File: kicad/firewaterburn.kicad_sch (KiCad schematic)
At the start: 7 parts, among them P101 USB_C_Plug_USB2.0, U101 TPD4E02B04DQA

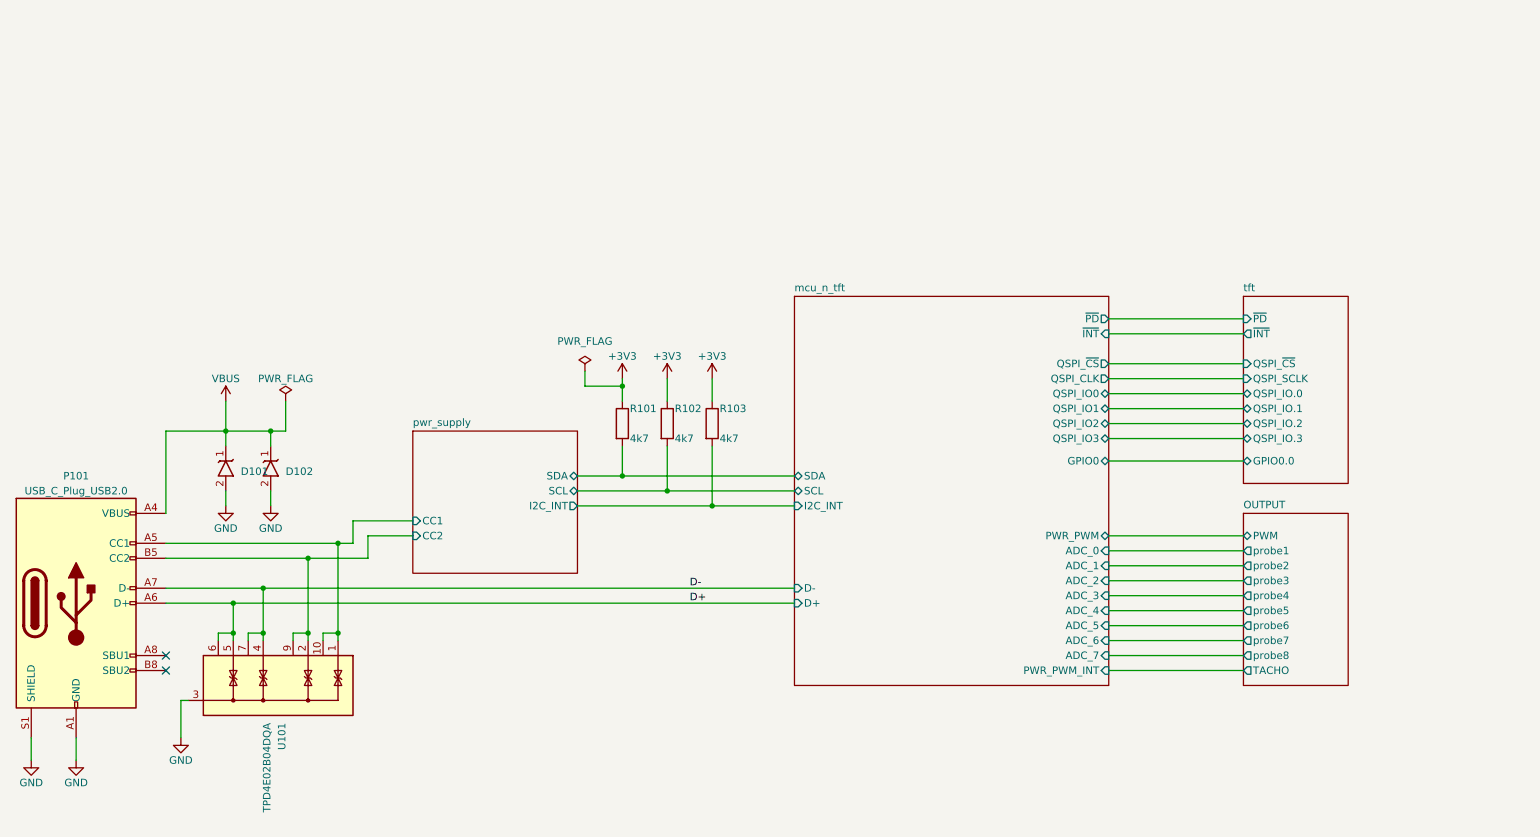
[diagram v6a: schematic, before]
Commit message: add nrf52840 board
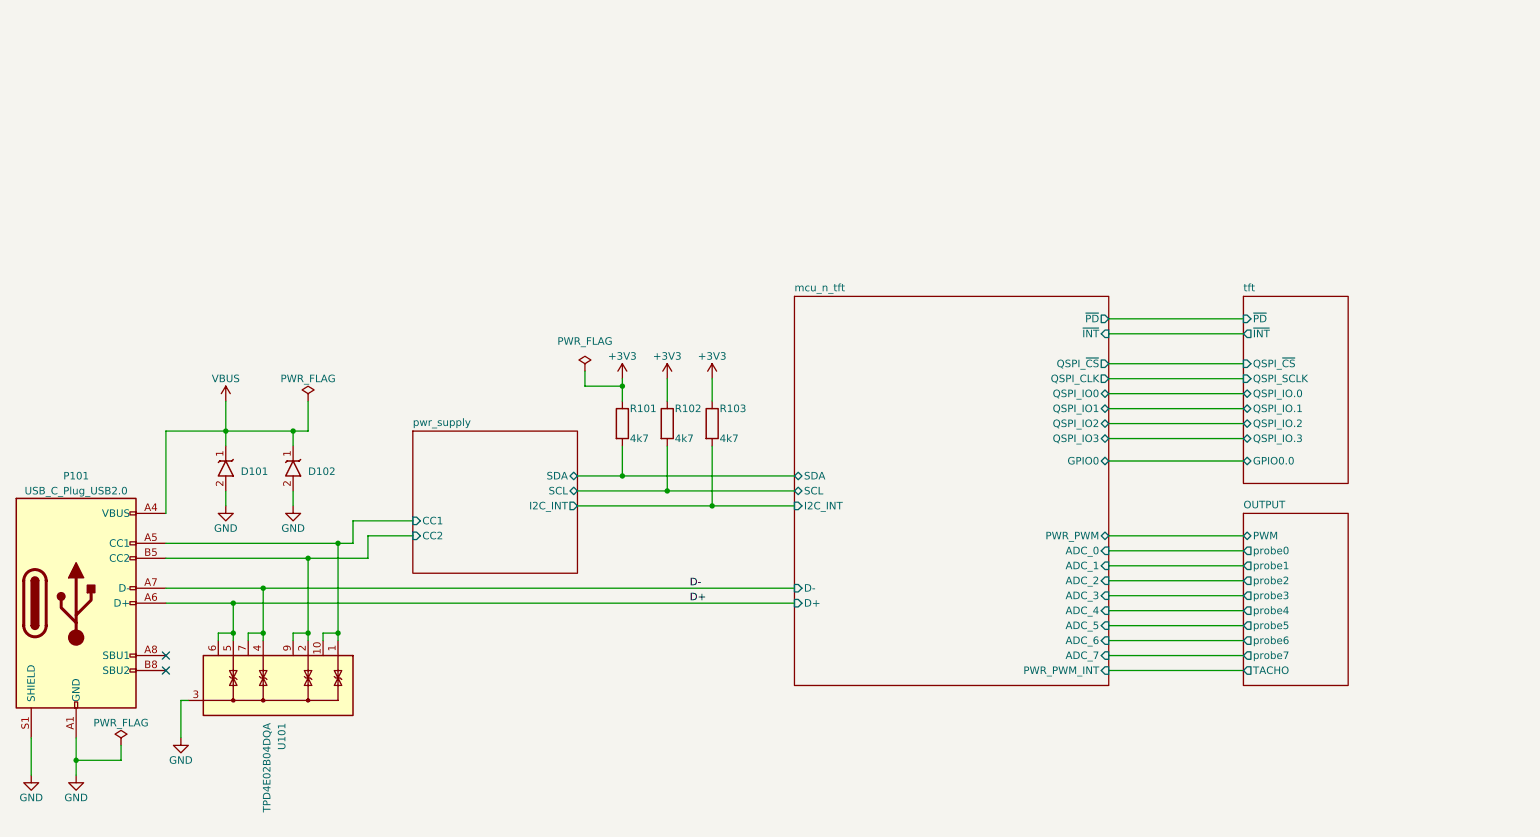
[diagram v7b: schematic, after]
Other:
- sheet OUTPUT ports: added probe0; removed probe8
- moved on the sheet: D102
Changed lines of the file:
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@@
   (junction (at 121.92 87.63) (diameter 0) (color 0 0 0 0)
   )
-  (junction (at 62.23 95.25) (diameter 0) (color 0 0 0 0)
+  (junction (at 29.21 151.13) (diameter 0) (color 0 0 0 0)
+  )
+  (junction (at 66.04 95.25) (diameter 0) (color 0 0 0 0)
   )
   (junction (at 137.16 107.95) (diameter 0) (color 0 0 0 0)
@@
     (stroke (width 0) (type default))
   )
-  (wire (pts (xy 21.59 151.13) (xy 21.59 147.32))
+  (wire (pts (xy 21.59 153.67) (xy 21.59 147.32))
     (stroke (width 0) (type default))
   )
@@
     (stroke (width 0) (type default))
   )
-  (wire (pts (xy 62.23 95.25) (xy 62.23 97.79))
+  (wire (pts (xy 66.04 95.25) (xy 66.04 97.79))
     (stroke (width 0) (type default))
   )
@@
     (stroke (width 0) (type default))
   )
-  (wire (pts (xy 62.23 105.41) (xy 62.23 107.95))
+  (wire (pts (xy 66.04 105.41) (xy 66.04 107.95))
+    (stroke (width 0) (type default))
+  )
+  (wire (pts (xy 36.83 148.59) (xy 36.83 151.13))
     (stroke (width 0) (type default))
   )
@@
     (stroke (width 0) (type default))
   )
+  (wire (pts (xy 29.21 151.13) (xy 36.83 151.13))
+    (stroke (width 0) (type default))
+  )
   (wire (pts (xy 60.96 129.54) (xy 60.96 130.81))
     (stroke (width 0) (type default))
@@
     (stroke (width 0) (type default))
   )
-  (wire (pts (xy 62.23 95.25) (xy 54.61 95.25))
+  (wire (pts (xy 66.04 95.25) (xy 54.61 95.25))
     (stroke (width 0) (type default))
   )
@@
     (stroke (width 0) (type default))
   )
-  (wire (pts (xy 64.77 95.25) (xy 62.23 95.25))
+  (wire (pts (xy 68.58 95.25) (xy 66.04 95.25))
     (stroke (width 0) (type default))
   )
@@
     (stroke (width 0) (type default))
   )
-  (wire (pts (xy 64.77 90.17) (xy 64.77 95.25))
+  (wire (pts (xy 68.58 90.17) (xy 68.58 95.25))
     (stroke (width 0) (type default))
   )
@@
   )
   (wire (pts (xy 44.45 95.25) (xy 54.61 95.25))
+    (stroke (width 0) (type default))
+  )
+  (wire (pts (xy 29.21 151.13) (xy 29.21 153.67))
     (stroke (width 0) (type default))
   )
@@
     )
   )
-  (symbol (lib_id "power:GND") (at 29.21 151.13 0) (unit 1)
-    (in_bom yes) (on_board yes) (dnp no)
-    (property "Reference" "#PWR0109" (at 29.21 157.48 0)
-      (effects (font (size 1.27 1.27)) hide)
-    )
-    (property "Value" "GND" (at 29.21 154.94 0)
-      (effects (font (size 1.27 1.27)))
-    )
-    (property "Footprint" "" (at 29.21 151.13 0)
-      (effects (font (size 1.27 1.27)) hide)
-    )
-    (property "Datasheet" "" (at 29.21 151.13 0)
+  (symbol (lib_id "power:GND") (at 29.21 153.67 0) (unit 1)
+    (in_bom yes) (on_board yes) (dnp no)
+    (property "Reference" "#PWR0109" (at 29.21 160.02 0)
+      (effects (font (size 1.27 1.27)) hide)
+    )
+    (property "Value" "GND" (at 29.21 157.48 0)
+      (effects (font (size 1.27 1.27)))
+    )
+    (property "Footprint" "" (at 29.21 153.67 0)
+      (effects (font (size 1.27 1.27)) hide)
+    )
+    (property "Datasheet" "" (at 29.21 153.67 0)
       (effects (font (size 1.27 1.27)) hide)
     )
@@
     )
   )
-  (symbol (lib_id "power:GND") (at 21.59 151.13 0) (unit 1)
-    (in_bom yes) (on_board yes) (dnp no)
-    (property "Reference" "#PWR0108" (at 21.59 157.48 0)
-      (effects (font (size 1.27 1.27)) hide)
-    )
-    (property "Value" "GND" (at 21.59 154.94 0)
-      (effects (font (size 1.27 1.27)))
-    )
-    (property "Footprint" "" (at 21.59 151.13 0)
-      (effects (font (size 1.27 1.27)) hide)
-    )
-    (property "Datasheet" "" (at 21.59 151.13 0)
+  (symbol (lib_id "power:GND") (at 21.59 153.67 0) (unit 1)
+    (in_bom yes) (on_board yes) (dnp no)
+    (property "Reference" "#PWR0108" (at 21.59 160.02 0)
+      (effects (font (size 1.27 1.27)) hide)
+    )
+    (property "Value" "GND" (at 21.59 157.48 0)
+      (effects (font (size 1.27 1.27)))
+    )
+    (property "Footprint" "" (at 21.59 153.67 0)
+      (effects (font (size 1.27 1.27)) hide)
+    )
+    (property "Datasheet" "" (at 21.59 153.67 0)
       (effects (font (size 1.27 1.27)) hide)
     )
@@
     )
   )
-  (symbol (lib_id "power:PWR_FLAG") (at 64.77 90.17 0) (unit 1)
-    (in_bom yes) (on_board yes) (dnp no)
-    (property "Reference" "#FLG0102" (at 64.77 88.265 0)
-      (effects (font (size 1.27 1.27)) hide)
-    )
-    (property "Value" "PWR_FLAG" (at 64.77 86.36 0)
-      (effects (font (size 1.27 1.27)))
-    )
-    (property "Footprint" "" (at 64.77 90.17 0)
-      (effects (font (size 1.27 1.27)) hide)
-    )
-    (property "Datasheet" "~" (at 64.77 90.17 0)
+  (symbol (lib_id "power:PWR_FLAG") (at 68.58 90.17 0) (unit 1)
+    (in_bom yes) (on_board yes) (dnp no)
+    (property "Reference" "#FLG0102" (at 68.58 88.265 0)
+      (effects (font (size 1.27 1.27)) hide)
+    )
+    (property "Value" "PWR_FLAG" (at 68.58 86.36 0)
+      (effects (font (size 1.27 1.27)))
+    )
+    (property "Footprint" "" (at 68.58 90.17 0)
+      (effects (font (size 1.27 1.27)) hide)
+    )
+    (property "Datasheet" "~" (at 68.58 90.17 0)
       (effects (font (size 1.27 1.27)) hide)
     )
@@
     )
   )
-  (symbol (lib_id "mylib_ic:ESDA25P35") (at 62.23 101.6 270) (unit 1)
+  (symbol (lib_id "mylib_ic:ESDA25P35") (at 66.04 101.6 270) (unit 1)
     (in_bom yes) (on_board yes) (dnp no) (fields_autoplaced)
-    (property "Reference" "D102" (at 64.77 102.108 90)
-      (effects (font (size 1.27 1.27)) (justify left))
-    )
-    (property "Value" "ESDA25P35" (at 59.69 101.6 0)
-      (effects (font (size 1.27 1.27)) hide)
-    )
-    (property "Footprint" "mylib_ic:D_0604_1610Metric" (at 62.23 101.6 0)
-      (effects (font (size 1.27 1.27)) hide)
-    )
-    (property "Datasheet" "" (at 62.23 101.6 0)
-      (effects (font (size 1.27 1.27)) hide)
-    )
-    (property "Digikey" "497-16913-1-ND" (at 62.23 101.6 90)
+    (property "Reference" "D102" (at 68.58 102.108 90)
+      (effects (font (size 1.27 1.27)) (justify left))
+    )
+    (property "Value" "ESDA25P35" (at 63.5 101.6 0)
+      (effects (font (size 1.27 1.27)) hide)
+    )
+    (property "Footprint" "mylib_ic:D_0604_1610Metric" (at 66.04 101.6 0)
+      (effects (font (size 1.27 1.27)) hide)
+    )
+    (property "Datasheet" "" (at 66.04 101.6 0)
+      (effects (font (size 1.27 1.27)) hide)
+    )
+    (property "Digikey" "497-16913-1-ND" (at 66.04 101.6 90)
       (effects (font (size 1.27 1.27)) hide)
     )
@@
     )
   )
-  (symbol (lib_id "power:GND") (at 62.23 107.95 0) (unit 1)
-    (in_bom yes) (on_board yes) (dnp no)
-    (property "Reference" "#PWR0106" (at 62.23 114.3 0)
-      (effects (font (size 1.27 1.27)) hide)
-    )
-    (property "Value" "GND" (at 62.23 111.76 0)
-      (effects (font (size 1.27 1.27)))
-    )
-    (property "Footprint" "" (at 62.23 107.95 0)
-      (effects (font (size 1.27 1.27)) hide)
-    )
-    (property "Datasheet" "" (at 62.23 107.95 0)
+  (symbol (lib_id "power:GND") (at 66.04 107.95 0) (unit 1)
+    (in_bom yes) (on_board yes) (dnp no)
+    (property "Reference" "#PWR0106" (at 66.04 114.3 0)
+      (effects (font (size 1.27 1.27)) hide)
+    )
+    (property "Value" "GND" (at 66.04 111.76 0)
+      (effects (font (size 1.27 1.27)))
+    )
+    (property "Footprint" "" (at 66.04 107.95 0)
+      (effects (font (size 1.27 1.27)) hide)
+    )
+    (property "Datasheet" "" (at 66.04 107.95 0)
       (effects (font (size 1.27 1.27)) hide)
     )
@@
         (path "/e63e39d7-6ac0-4ffd-8aa3-1841a4541b55"
           (reference "#FLG0101") (unit 1)
+        )
+      )
+    )
+  )
+  (symbol (lib_id "power:PWR_FLAG") (at 36.83 148.59 0) (unit 1)
+    (in_bom yes) (on_board yes) (dnp no)
+    (property "Reference" "#FLG0103" (at 36.83 146.685 0)
+      (effects (font (size 1.27 1.27)) hide)
+    )
+    (property "Value" "PWR_FLAG" (at 36.83 144.78 0)
+      (effects (font (size 1.27 1.27)))
+    )
+    (property "Footprint" "" (at 36.83 148.59 0)
+      (effects (font (size 1.27 1.27)) hide)
+    )
+    (property "Datasheet" "~" (at 36.83 148.59 0)
+      (effects (font (size 1.27 1.27)) hide)
+    )
+    (pin "1")
+    (instances
+      (project "firewaterburn"
+        (path "/e63e39d7-6ac0-4ffd-8aa3-1841a4541b55"
+          (reference "#FLG0103") (unit 1)
         )
       )
@@
       (effects (font (size 1.27 1.27)) (justify left top) hide)
     )
-    (pin "probe6" output (at 227.33 128.27 180)
-      (effects (font (size 1.27 1.27)) (justify left))
-    )
-    (pin "probe3" output (at 227.33 120.65 180)
-      (effects (font (size 1.27 1.27)) (justify left))
-    )
-    (pin "probe2" output (at 227.33 118.11 180)
-      (effects (font (size 1.27 1.27)) (justify left))
-    )
-    (pin "probe1" output (at 227.33 115.57 180)
-      (effects (font (size 1.27 1.27)) (justify left))
-    )
-    (pin "probe4" output (at 227.33 123.19 180)
-      (effects (font (size 1.27 1.27)) (justify left))
-    )
-    (pin "probe5" output (at 227.33 125.73 180)
+    (pin "probe6" output (at 227.33 130.81 180)
+      (effects (font (size 1.27 1.27)) (justify left))
+    )
+    (pin "probe3" output (at 227.33 123.19 180)
+      (effects (font (size 1.27 1.27)) (justify left))
+    )
+    (pin "probe2" output (at 227.33 120.65 180)
+      (effects (font (size 1.27 1.27)) (justify left))
+    )
+    (pin "probe1" output (at 227.33 118.11 180)
+      (effects (font (size 1.27 1.27)) (justify left))
+    )
+    (pin "probe4" output (at 227.33 125.73 180)
+      (effects (font (size 1.27 1.27)) (justify left))
+    )
+    (pin "probe5" output (at 227.33 128.27 180)
       (effects (font (size 1.27 1.27)) (justify left))
     )
@@
       (effects (font (size 1.27 1.27)) (justify left))
     )
-    (pin "probe7" output (at 227.33 130.81 180)
-      (effects (font (size 1.27 1.27)) (justify left))
-    )
-    (pin "probe8" output (at 227.33 133.35 180)
-      (effects (font (size 1.27 1.27)) (justify left))
-    )
+    (pin "probe7" output (at 227.33 133.35 180)
+      (effects (font (size 1.27 1.27)) (justify left))
+    )
+    (pin "probe0" output (at 227.33 115.57 180)
+      (effects (font (size 1.27 1.27)) (justify left))
+    )

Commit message: rework board
add nrf 7002
add oled display
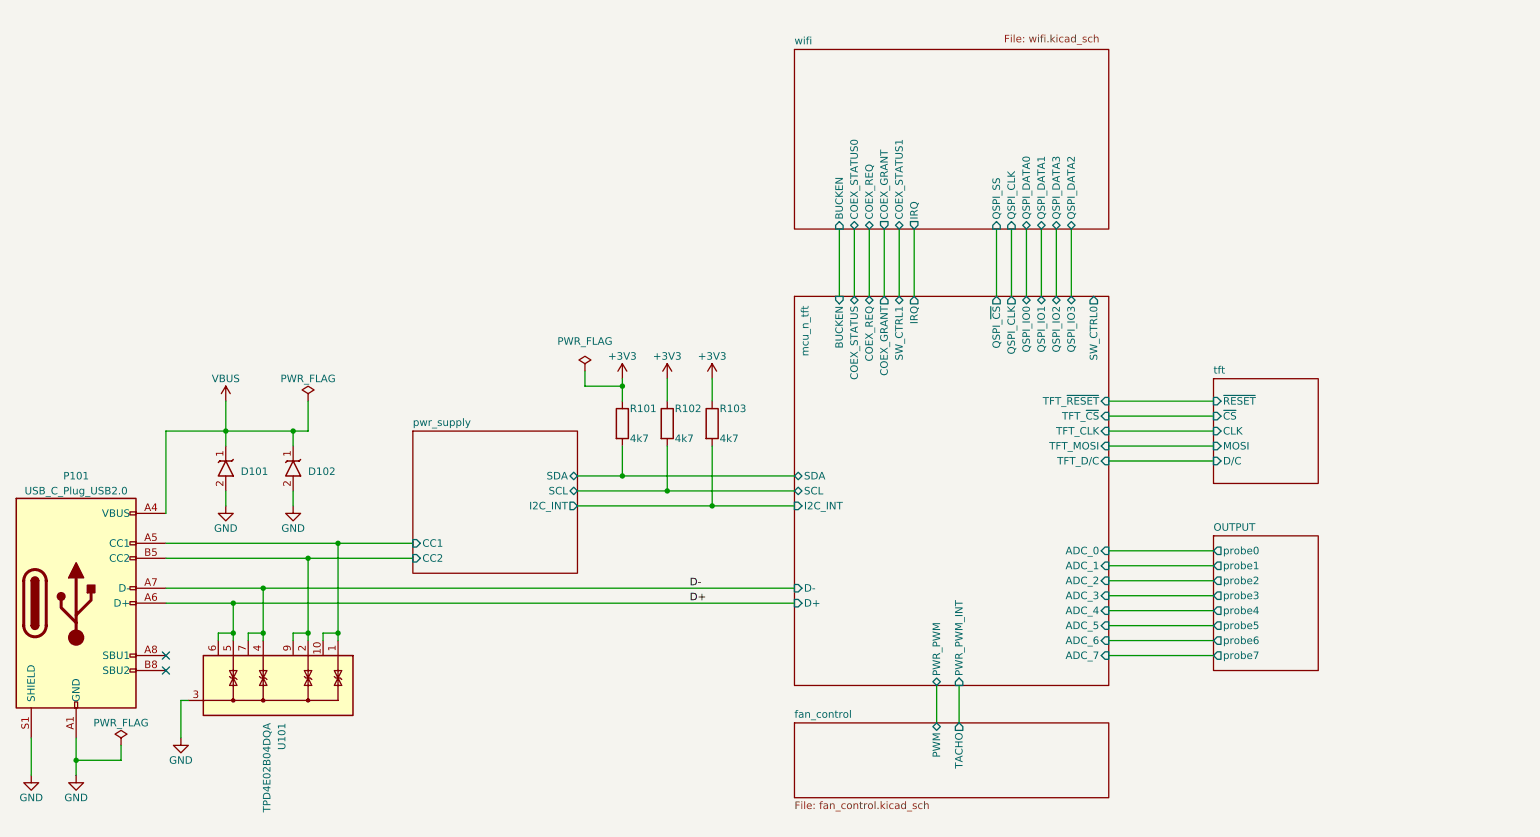
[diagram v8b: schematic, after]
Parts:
- R101, R102, R103: footprint Resistor_SMD:R_0603_1608Metric -> Resistor_SMD:R_0402_1005Metric; Digikey 311-4.70KHRCT-ND -> 13-RC0402FR-134K7LTR-ND
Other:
- added sheet fan_control (fan_control.kicad_sch)
- added sheet wifi (wifi.kicad_sch)
- sheet OUTPUT ports: added none; removed PWM, TACHO
- sheet mcu_n_tft ports: added BUCKEN, COEX_GRANT, COEX_REQ, COEX_STATUS, IRQ, SW_CTRL0, SW_CTRL1, TFT_CLK, TFT_D/C, TFT_MOSI, TFT_~{CS}, TFT_~{RESET}; removed GPIO0, ~{INT}, ~{PD}
- sheet tft ports: added CLK, D/C, MOSI, ~{CS}, ~{RESET}; removed GPIO0.0, QSPI_IO.0, QSPI_IO.1, QSPI_IO.2, QSPI_IO.3, QSPI_SCLK, QSPI_~{CS}, ~{INT}, ~{PD}
- title: (none) -> Firewaterburn
